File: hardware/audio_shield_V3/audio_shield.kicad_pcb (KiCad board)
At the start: 2 copper layers, 129.5 x 129.4 mm, 63 parts, among them J1 CONN_10_LEFT, J2 CONN_10_RIGHT, J9 SWD_TC2030, Q1 BS170F, U1 STM32F446RETx, U2 DS28E05R+T, U3 DS28E05R+T

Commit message: Update hardware V3 with correct version
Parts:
- EE1, PA2, PC3: moved to B.Cu
- moved C9 1.17 mm to (132.8, 101.4), turned to 0 degrees
- turned D1 to 270 degrees
- turned D2 to 0 degrees
- turned D3 to 270 degrees
- turned D4 to 180 degrees
- turned PA2 to 270 degrees
- turned PC3 to 270 degrees
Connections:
- D1 pad 1: Net-(D1-Pad1) -> GND
- D1 pad 2: GND -> Net-(D1-Pad2)
- D2 pad 1: Net-(D2-Pad1) -> GND
- D2 pad 2: GND -> Net-(D2-Pad2)
- D3 pad 1: Net-(D3-Pad1) -> GND
- D3 pad 2: GND -> Net-(D3-Pad2)
- D4 pad 1: Net-(D4-Pad1) -> GND
- D4 pad 2: GND -> Net-(D4-Pad2)
- R11 pad 1: Net-(D1-Pad1) -> Net-(D1-Pad2)
- R12 pad 1: Net-(D2-Pad1) -> Net-(D2-Pad2)
- R13 pad 1: Net-(D3-Pad1) -> Net-(D3-Pad2)
- R14 pad 1: Net-(D4-Pad1) -> Net-(D4-Pad2)
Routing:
- net /I2S1_WS: track 17.5 -> 157.6 mm, vias 0 -> 5
- net /I2S1_SD: track 0.00 -> 115.1 mm, vias 0 -> 6
- net /SPI2_CK: track 1.60 -> 85.5 mm, vias 0 -> 3
- net /I2S1_CK: track 72.8 -> 154.9 mm, vias 5 -> 9
- net Net-(D2-Pad1): track 54.2 -> 0.00 mm, vias 1 -> 0
- net /SPI2_MOSI: track 39.3 -> 88.2 mm, vias 3 -> 4
- net /SPI2_MISO: track 38.0 -> 78.0 mm, vias 4 -> 3
- net Net-(D3-Pad2): track 0.00 -> 35.2 mm, vias 0 -> 1
- net Net-(D1-Pad2): track 0.00 -> 34.8 mm, vias 0 -> 1
- net Net-(D1-Pad1): track 34.8 -> 0.00 mm, vias 1 -> 0
- net GND: track 26.8 -> 59.3 mm, vias 16 -> 18
- net /LED4: track 0.00 -> 31.5 mm, vias 0 -> 1
- net Net-(D4-Pad2): track 0.00 -> 30.8 mm, vias 0 -> 1
- net Net-(MK3-Pad6): track 0.00 -> 30.3 mm
- net /SPI2_NSS: track 1.60 -> 31.1 mm, vias 0 -> 1
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
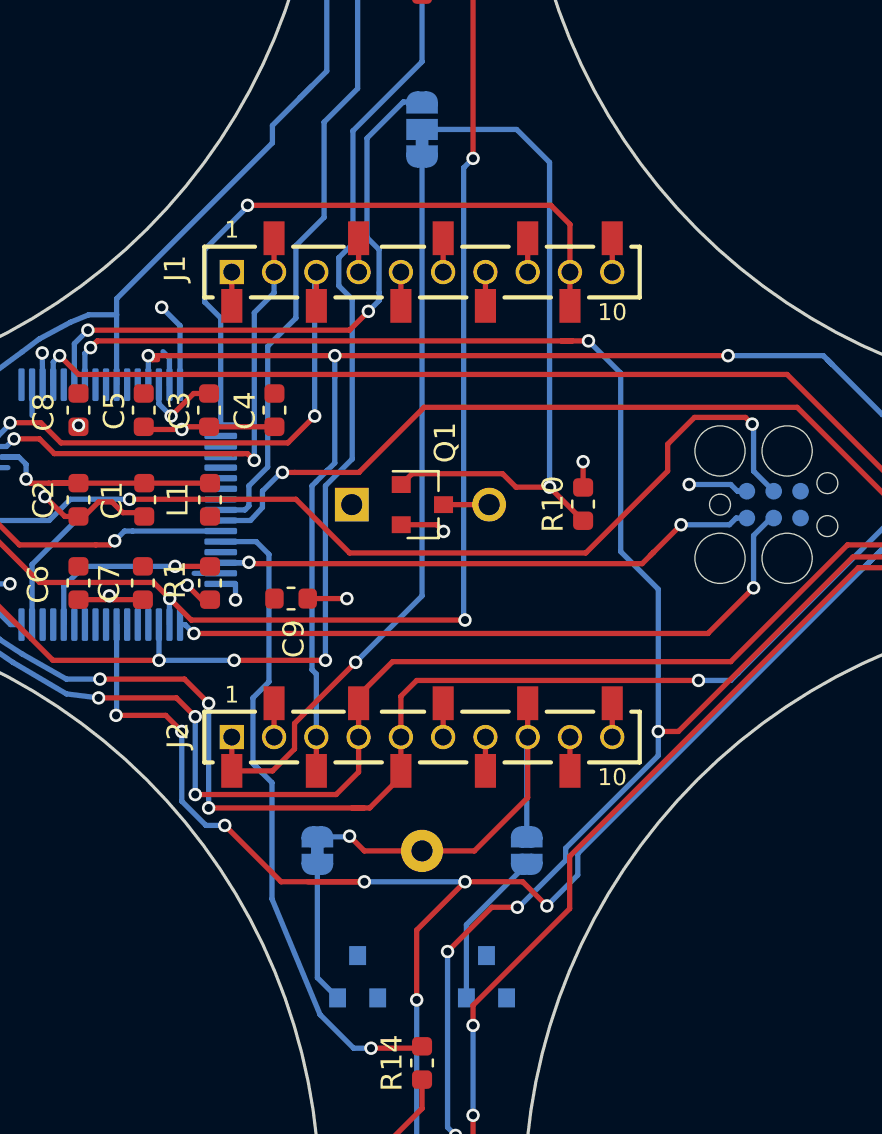
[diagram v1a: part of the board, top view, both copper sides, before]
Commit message: Correct PCB after testing the HW
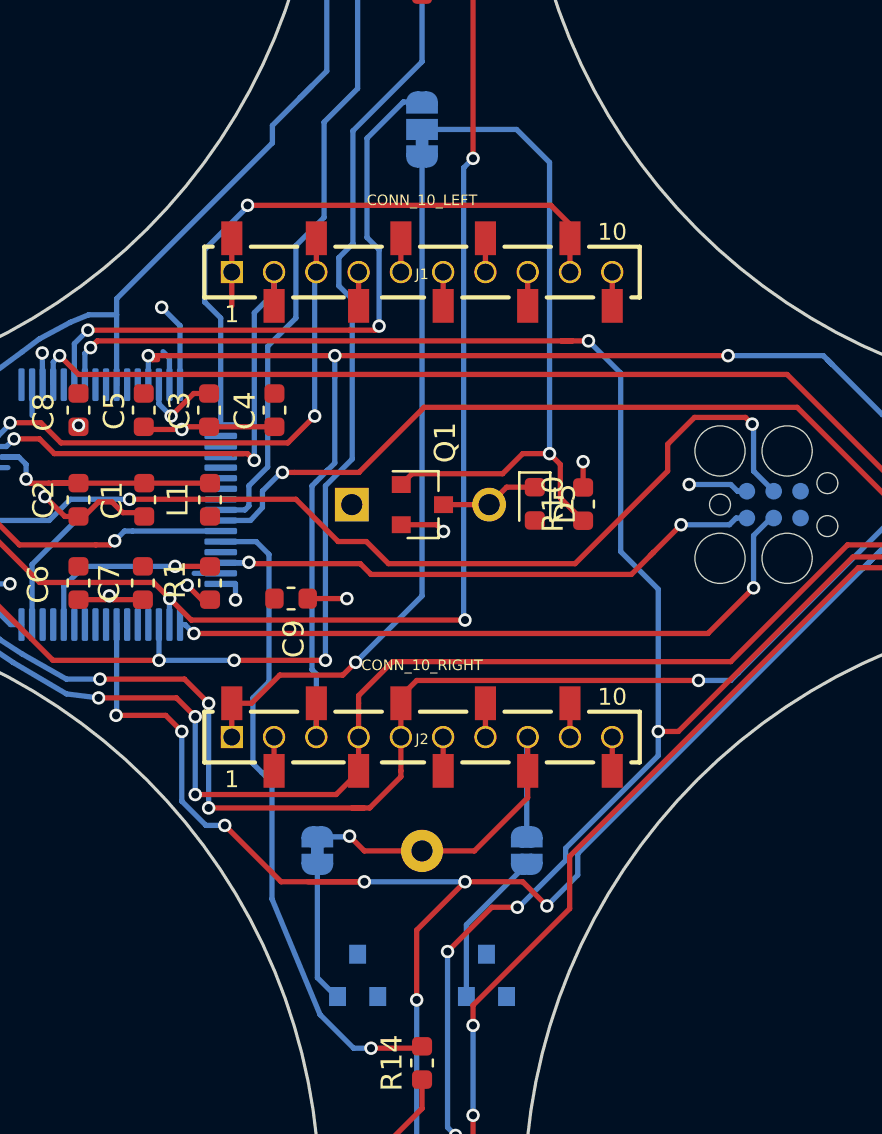
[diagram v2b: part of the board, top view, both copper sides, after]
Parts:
- added D5: DIODE, Diode_SMD:D_0603_1608Metric, F.Cu at (144.3, 97.0)
- J1, J2: footprint audio_shield:BF090-10-X-B1 -> audio_shield:BF090-10-X-B2
- U2, U3: value DS28E05R+T -> DS2401Z
- moved U2 0.06 mm to (142.0, 119.3)
- moved U3 0.06 mm to (136.0, 119.3)
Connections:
- U2 pad 1: GND -> (no net)
- U2 pad 3: (no net) -> GND
- U3 pad 1: GND -> (no net)
- U3 pad 3: (no net) -> GND
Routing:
- net Net-(BZ1-Pad2): track 2.16 -> 4.85 mm
- net /CF_Buzzer: track 35.6 -> 33.5 mm
- net /SPI2_NSS: track 31.1 -> 29.5 mm
- net /EEPROM: track 20.9 -> 19.3 mm
- net +3V0: track 21.4 -> 23.0 mm
- net /AD_Buzzer: track 28.4 -> 29.1 mm
